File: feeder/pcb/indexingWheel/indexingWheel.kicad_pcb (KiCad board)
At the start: 2 copper layers, 43 x 43 mm, 4 parts

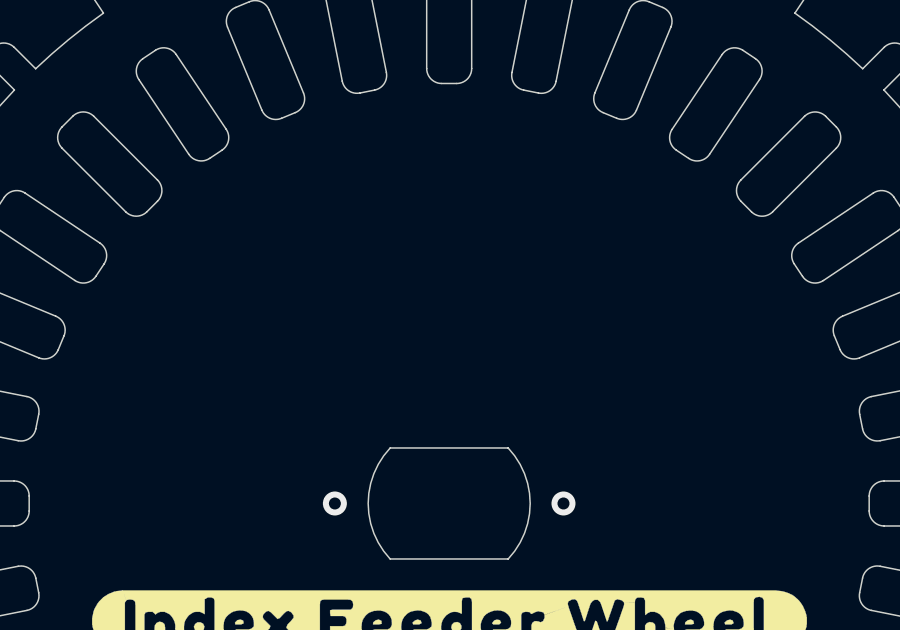
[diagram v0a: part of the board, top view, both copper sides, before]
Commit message: Add Index logo to feeder floor and wheel
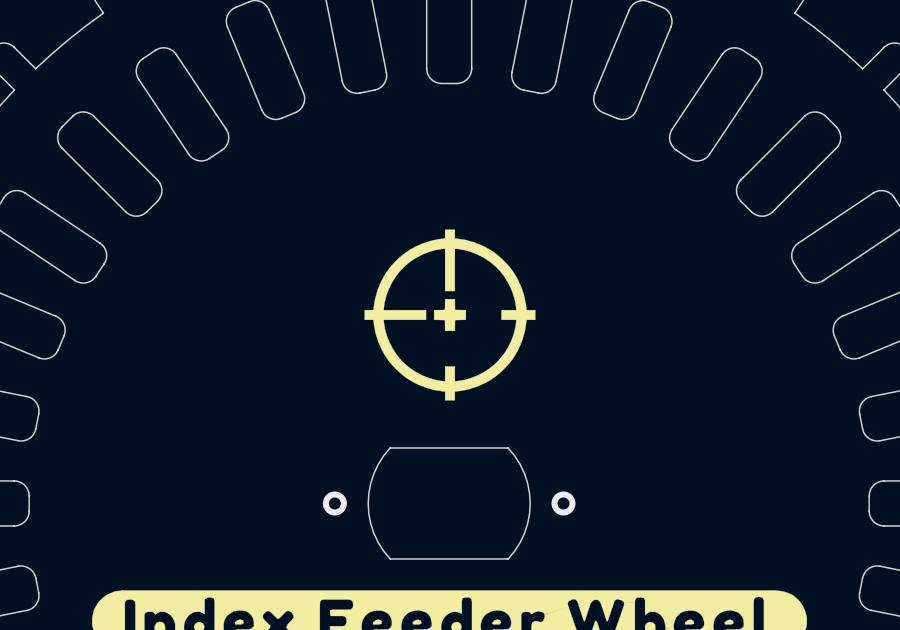
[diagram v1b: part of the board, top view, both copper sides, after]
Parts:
- added G***: LOGO, index:logo, B.Cu at (0.06, -6.29)
- added G***: LOGO, index:logo, F.Cu at (0.02, -6.29)

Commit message: Rotate Index logo
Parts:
- turned G*** to 180 degrees
